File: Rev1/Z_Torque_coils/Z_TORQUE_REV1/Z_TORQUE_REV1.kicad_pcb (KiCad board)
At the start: 2 copper layers, 95.9 x 90.2 mm, 0 parts

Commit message: changed layer stack
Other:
- copper layers 2 -> 6
- rule pad_to_mask_clearance: 0 -> 0.0508
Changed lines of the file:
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@@
 (kicad_pcb (version 20221018) (generator pcbnew)
   (general
-    (thickness 1.6)
+    (thickness 1.07)
   )
   (paper "A4")
   (layers
     (0 "F.Cu" signal)
+    (1 "In1.Cu" signal)
+    (2 "In2.Cu" signal)
+    (3 "In3.Cu" signal)
+    (4 "In4.Cu" signal)
     (31 "B.Cu" signal)
     (32 "B.Adhes" user "B.Adhesive")
@@
   )
   (setup
-    (pad_to_mask_clearance 0)
+    (stackup
+      (layer "F.SilkS" (type "Top Silk Screen"))
+      (layer "F.Paste" (type "Top Solder Paste"))
+      (layer "F.Mask" (type "Top Solder Mask") (thickness 0.01))
+      (layer "F.Cu" (type "copper") (thickness 0.05))
+      (layer "dielectric 1" (type "prepreg") (thickness 0.22 locked) (material "FR4") (epsilon_r 4.5) (loss_tangent 0.02))
+      (layer "In1.Cu" (type "copper") (thickness 0.02))
+      (layer "dielectric 2" (type "core") (thickness 0.4 locked) (material "FR4") (epsilon_r 4.5) (loss_tangent 0.02))
+      (layer "In2.Cu" (type "copper") (thickness 0.02))
+      (layer "dielectric 3" (type "prepreg") (thickness 0.22 locked) (material "FR4") (epsilon_r 4.5) (loss_tangent 0.02))
+      (layer "In3.Cu" (type "copper") (thickness 0.035))
+      (layer "dielectric 4" (type "core") (thickness 0) (material "FR4") (epsilon_r 4.5) (loss_tangent 0.02))
+      (layer "In4.Cu" (type "copper") (thickness 0.035))
+      (layer "dielectric 5" (type "prepreg") (thickness 0) (material "FR4") (epsilon_r 4.5) (loss_tangent 0.02))
+      (layer "B.Cu" (type "copper") (thickness 0.05))
+      (layer "B.Mask" (type "Bottom Solder Mask") (thickness 0.01))
+      (layer "B.Paste" (type "Bottom Solder Paste"))
+      (layer "B.SilkS" (type "Bottom Silk Screen"))
+      (copper_finish "None")
+      (dielectric_constraints no)
+    )
+    (pad_to_mask_clearance 0.0508)
     (pcbplotparams
       (layerselection 0x00010fc_ffffffff)

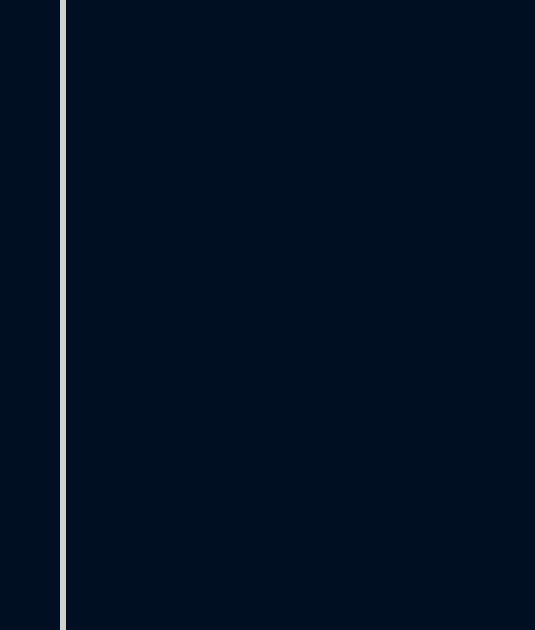
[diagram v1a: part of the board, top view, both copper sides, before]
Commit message: Z torque coils done for 2 layers 54 loops each
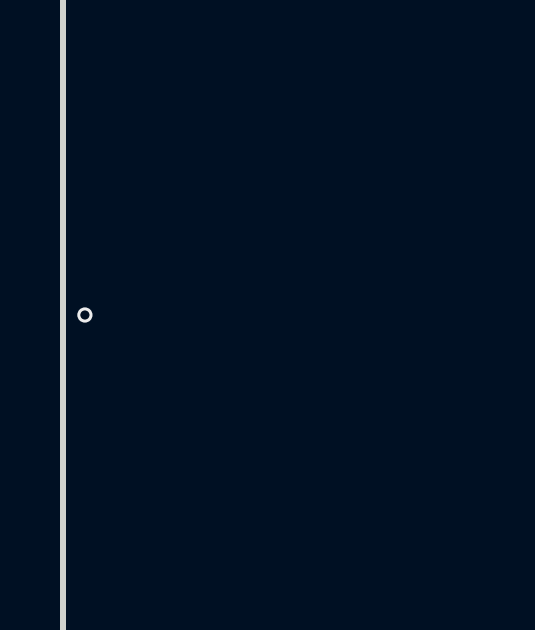
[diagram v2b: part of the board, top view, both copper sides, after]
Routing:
- net coils: track 0.00 -> 33572.5 mm, vias 0 -> 1

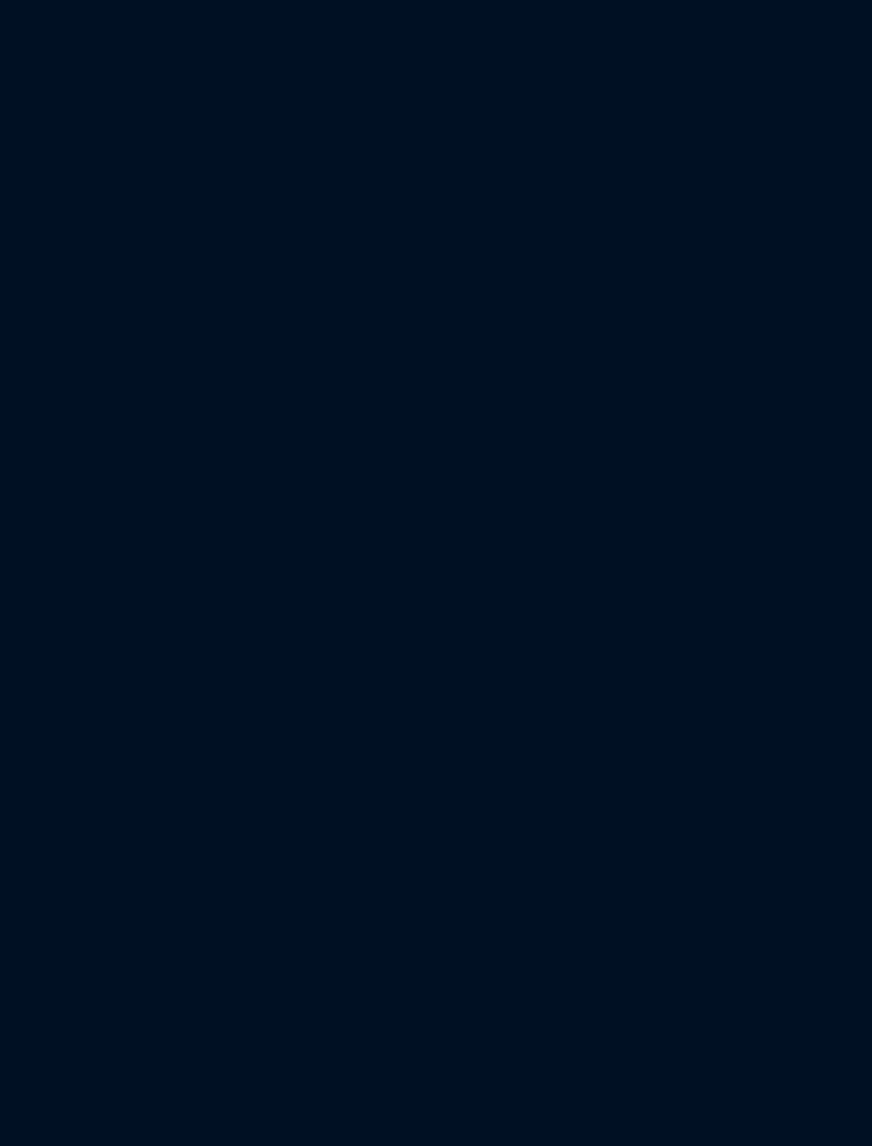
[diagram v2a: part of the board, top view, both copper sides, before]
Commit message: added scehmatic
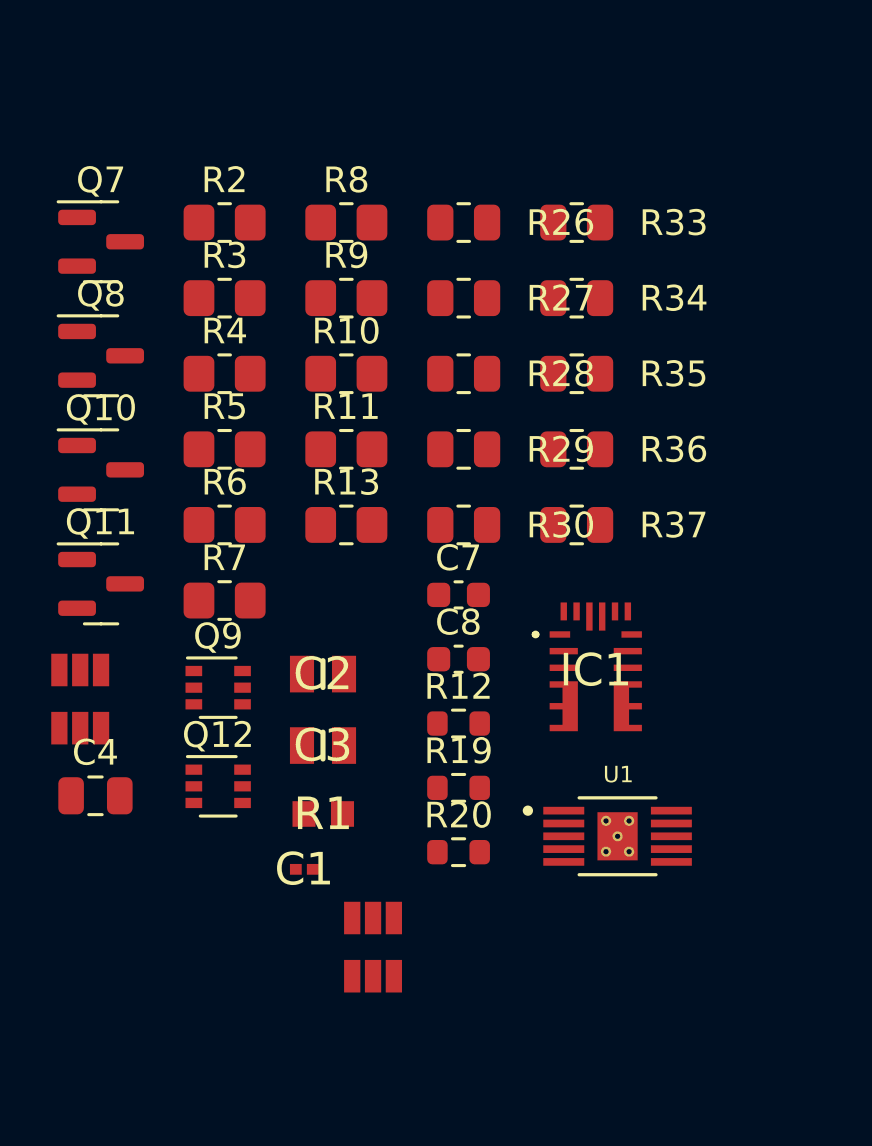
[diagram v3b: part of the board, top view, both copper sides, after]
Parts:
- added C1: GRM033R60J224KE15D, AA_AUTO_LOADER:CAPC0603X33N, F.Cu at (71.4, 102.8)
- added C2: CL21A106KOQNNNE, AA_AUTO_LOADER:CAPC2012X140N, F.Cu at (72.2, 95.2)
- added C3: CL21A106KOQNNNE, AA_AUTO_LOADER:CAPC2012X140N, F.Cu at (72.2, 98.0)
- added C4: 0.1uF, Capacitor_SMD:C_0805_2012Metric, F.Cu at (63.3, 100.0)
- added C7: 10nF, Capacitor_SMD:C_0603_1608Metric, F.Cu at (77.5, 92.1)
- added C8: 10nF, Capacitor_SMD:C_0603_1608Metric, F.Cu at (77.5, 94.6)
- added IC1: MPM3610AGQV-Z, AA_AUTO_LOADER:MPM3610AGQVZ, F.Cu at (82.8, 95.2)
- added JP1: ~, SparkFun-Jumper:SMT-JUMPER_3_NO_NO-SILK, F.Cu at (62.7, 95.1)
- added JP2: ~, SparkFun-Jumper:SMT-JUMPER_3_NO_NO-SILK, F.Cu at (62.7, 97.3)
- added JP3: ~, SparkFun-Jumper:SMT-JUMPER_3_NO_NO-SILK, F.Cu at (74.1, 104.7)
- added JP4: ~, SparkFun-Jumper:SMT-JUMPER_3_NO_NO-SILK, F.Cu at (74.1, 107.0)
- added Q10: BSS138, Package_TO_SOT_SMD:SOT-23, F.Cu at (63.5, 87.2)
- added Q11: BSS138, Package_TO_SOT_SMD:SOT-23, F.Cu at (63.5, 91.7)
- added Q12: MBT2222ADW1T1, Package_TO_SOT_SMD:SOT-363_SC-70-6, F.Cu at (68.1, 99.6)
- added Q7: BSS138, Package_TO_SOT_SMD:SOT-23, F.Cu at (63.5, 78.3)
- added Q8: BSS138, Package_TO_SOT_SMD:SOT-23, F.Cu at (63.5, 82.8)
- added Q9: MBT2222ADW1T1, Package_TO_SOT_SMD:SOT-363_SC-70-6, F.Cu at (68.1, 95.8)
- added R1: RMCF0603FT19K1, AA_AUTO_LOADER:RESC1608X55N, F.Cu at (72.2, 100.7)
- added R10: 0, Resistor_SMD:R_0805_2012Metric_Pad1.20x1.40mm_HandSolder, F.Cu at (73.1, 83.5)
- added R11: 0, Resistor_SMD:R_0805_2012Metric_Pad1.20x1.40mm_HandSolder, F.Cu at (73.1, 86.5)
- added R12: 100K, Resistor_SMD:R_0603_1608Metric, F.Cu at (77.5, 97.2)
- added R13: 100K, Resistor_SMD:R_0805_2012Metric_Pad1.20x1.40mm_HandSolder, F.Cu at (73.1, 89.4)
- added R19: 0, Resistor_SMD:R_0603_1608Metric, F.Cu at (77.5, 99.7)
- added R2: 100K, Resistor_SMD:R_0805_2012Metric_Pad1.20x1.40mm_HandSolder, F.Cu at (68.3, 77.6)
- added R20: 0, Resistor_SMD:R_0603_1608Metric, F.Cu at (77.5, 102.2)
- added R26: 10K, Resistor_SMD:R_0805_2012Metric, F.Cu at (77.7, 77.6)
- added R27: 600, Resistor_SMD:R_0805_2012Metric, F.Cu at (77.7, 80.5)
- added R28: 10K, Resistor_SMD:R_0805_2012Metric, F.Cu at (77.7, 83.5)
- added R29: 10K, Resistor_SMD:R_0805_2012Metric, F.Cu at (77.7, 86.5)
- added R3: 0, Resistor_SMD:R_0805_2012Metric_Pad1.20x1.40mm_HandSolder, F.Cu at (68.3, 80.5)
- added R30: 100K, Resistor_SMD:R_0805_2012Metric, F.Cu at (77.7, 89.4)
- added R33: 10K, Resistor_SMD:R_0805_2012Metric, F.Cu at (82.1, 77.6)
- added R34: 600, Resistor_SMD:R_0805_2012Metric, F.Cu at (82.1, 80.5)
- added R35: 10K, Resistor_SMD:R_0805_2012Metric, F.Cu at (82.1, 83.5)
- added R36: 10K, Resistor_SMD:R_0805_2012Metric, F.Cu at (82.1, 86.5)
- added R37: 100K, Resistor_SMD:R_0805_2012Metric, F.Cu at (82.1, 89.4)
- added R4: 0, Resistor_SMD:R_0805_2012Metric_Pad1.20x1.40mm_HandSolder, F.Cu at (68.3, 83.5)
- added R5: 0, Resistor_SMD:R_0805_2012Metric_Pad1.20x1.40mm_HandSolder, F.Cu at (68.3, 86.5)
- added R6: 0, Resistor_SMD:R_0805_2012Metric_Pad1.20x1.40mm_HandSolder, F.Cu at (68.3, 89.4)
- added R7: 0, Resistor_SMD:R_0805_2012Metric_Pad1.20x1.40mm_HandSolder, F.Cu at (68.3, 92.3)
- added R8: 0, Resistor_SMD:R_0805_2012Metric_Pad1.20x1.40mm_HandSolder, F.Cu at (73.1, 77.6)
- added R9: 0, Resistor_SMD:R_0805_2012Metric_Pad1.20x1.40mm_HandSolder, F.Cu at (73.1, 80.5)
- added U1: DRV8830DGQ, DRV8830DGQ:IC_XTR111AIDGQR, F.Cu at (83.7, 101.5)

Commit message: incremental update
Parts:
- removed the R10 at (73.1, 83.5)
- removed the R11 at (73.1, 86.5)
- removed the R8 at (73.1, 77.6)
- removed the R9 at (73.1, 80.5)
- added J1: F3311A7H121014E200, AA_AUTO_LOADER:F3311A7H121014E200, B.Cu at (186.7, 66.4)
- added J2: F3311A7H121014E200, AA_AUTO_LOADER:F3311A7H121014E200, B.Cu at (174.8, 66.4)
- C1, C2, C3, C4, IC1, R1, R2, R3, R4, R5, R6, R7, U1: moved to B.Cu
- C5: renamed from C7; moved to B.Cu
- C6: renamed from C8; moved to B.Cu
- JP1: renamed from JP4; moved to B.Cu
- JP2: renamed from JP3; moved to B.Cu
- JP3: renamed from JP1; moved to B.Cu
- JP4: renamed from JP2; moved to B.Cu
- Q1: renamed from Q7; moved to B.Cu
- Q2: renamed from Q8; moved to B.Cu
- Q3: renamed from Q9; moved to B.Cu
- Q4: renamed from Q10; moved to B.Cu
- Q5: renamed from Q11; moved to B.Cu
- Q6: renamed from Q12; moved to B.Cu
- R10: renamed from R26; moved to B.Cu
- R11: renamed from R27; moved to B.Cu
- R12: renamed from R28; moved to B.Cu
- R13: renamed from R29; moved to B.Cu
- R14: renamed from R30; moved to B.Cu
- R15: renamed from R19; moved to B.Cu
- R16: renamed from R20; moved to B.Cu
- R17: renamed from R33; moved to B.Cu
- R18: renamed from R34; moved to B.Cu
- R19: renamed from R35; moved to B.Cu
- R20: renamed from R36; moved to B.Cu
- R21: renamed from R37; moved to B.Cu
- R8: renamed from R12; moved to B.Cu
- R9: renamed from R13; moved to B.Cu
- moved C2 98.5 mm to (170.5, 90.5), turned to 90 degrees
- moved R9 95.4 mm to (168.5, 90.9), turned to 90 degrees
- moved R2 92.0 mm to (158.6, 95.0), turned to -90 degrees
- moved R8 91.6 mm to (169.1, 97.8), turned to -90 degrees
- moved Q1 90.1 mm to (153.6, 82.5)
- moved Q3 86.7 mm to (154.3, 86.5), turned to 90 degrees
- moved R1 86.5 mm to (158.7, 98.6), turned to -90 degrees
- moved Q2 85.8 mm to (149.3, 83.4)
- moved C1 85.3 mm to (156.4, 94.4), turned to -90 degrees
- moved JP2 84.3 mm to (158.4, 103.2), turned to -90 degrees
- moved JP1 81.8 mm to (155.9, 105.2), turned to -90 degrees
- moved R15 81.1 mm to (157.8, 88.4)
- moved R10 81.0 mm to (158.5, 82.9)
- moved R12 80.8 mm to (158.5, 80.5), turned to 180 degrees
- moved R13 80.8 mm to (158.5, 85.4)
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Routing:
- net coils: track 33572.5 -> 84026.2 mm, vias 1 -> 6
- net +3.3V: track 0.00 -> 120.1 mm, vias 0 -> 2
- net VBATT: track 0.00 -> 93.6 mm
- net SDA1_b4iso: track 0.00 -> 89.2 mm
- net SDA_TORQUE: track 0.00 -> 76.8 mm, vias 0 -> 2
- net SCL1_b4iso: track 0.00 -> 67.8 mm
- net SCL_TORQUE: track 0.00 -> 43.6 mm, vias 0 -> 2
- net VSOLAR: track 0.00 -> 34.4 mm
- net 5V: track 0.00 -> 29.3 mm
- net GND: track 0.00 -> 28.9 mm
- net Net-(Q1-D): track 0.00 -> 22.3 mm
- net Net-(JP3-A): track 0.00 -> 21.8 mm, vias 0 -> 2
- net Net-(IC1-FB): track 0.00 -> 21.7 mm
- net Net-(U1-ISENSE): track 0.00 -> 17.3 mm
- net Net-(JP3-B): track 0.00 -> 17.1 mm
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
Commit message: final signoff by nischal
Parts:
- added .: ., argus:Argus LOGO, F.Cu at (140.4, 105.2)
- added .: ., argus:Argus LOGO, B.Cu at (183.2, 114.6)
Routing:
- net coils: track 84026.2 -> 83639.0 mm
- net GND: track 28.9 -> 34.5 mm, vias 0 -> 56
- net Net-(IC1-FB): track 21.7 -> 23.3 mm
- net Net-(JP2-C): track 7.52 -> 9.00 mm
- added copper zone on B.Cu, net GND
- added copper zone on F.Cu, net GND
- added copper zone on In1.Cu, net GND
- added copper zone on In2.Cu, net GND
- added copper zone on In3.Cu, net GND
- added copper zone on In4.Cu, net GND
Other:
- board text added: "DESIGNED BY NISCHAL"
- board text added: "Z_TORQUE_COIL_BOARD REV 1.0 ARGUS-1"

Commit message: made layer changes and sent out the board
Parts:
- added ?: , , F.Cu at (154.8, 71.9)
- added ?: , , F.Cu at (175.0, 84.8)
- added ?: , , F.Cu at (175.1, 81.0)
- added ?: , , F.Cu at (157.8, 71.8)
- added ?: , , F.Cu at (150.2, 96.9)
- added ?: , , F.Cu at (166.3, 87.5)
- added ?: , , F.Cu at (166.3, 82.7)
- moved . 28.6 mm to (168.6, 110.1)
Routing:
- net coils: track 83639.0 -> 50068.4 mm, vias 6 -> 4
- net SCL1_b4iso: track 67.8 -> 82.4 mm, vias 0 -> 1
- net SDA_TORQUE: track 76.8 -> 69.6 mm
- net +3.3V: track 120.0 -> 126.2 mm
- net 5V: track 29.3 -> 35.1 mm
- net SDA1_b4iso: track 89.2 -> 94.0 mm
- net VBATT: track 93.6 -> 98.2 mm
- net SCL_TORQUE: track 43.6 -> 42.0 mm
- removed copper zone on In3.Cu, net GND
- removed copper zone on In4.Cu, net GND
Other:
- copper layers 6 -> 4
- board text added: "3V3"
- board text added: "5V"
- board text added: "ADDR SET"
- board text added: "COIL DIR"
- board text added: "GND"
- board text added: "I_Sense 0-1 OHM"
- board text added: "SCL_B"
- board text added: "SDA_B"
- board text added: "VBAT"
